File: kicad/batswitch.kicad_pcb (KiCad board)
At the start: 2 copper layers, 45.3 x 39.4 mm, 45 parts, among them J1 -VIN+, J2 -VOUT+, J3 DBG, J4 I2C_AUX, J5 I2C_DISP, Q1 SUD45P03-09, Q2 BSS84, Q3 SUD45P03-09, Q4 AO3401A, Q5 BSS138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

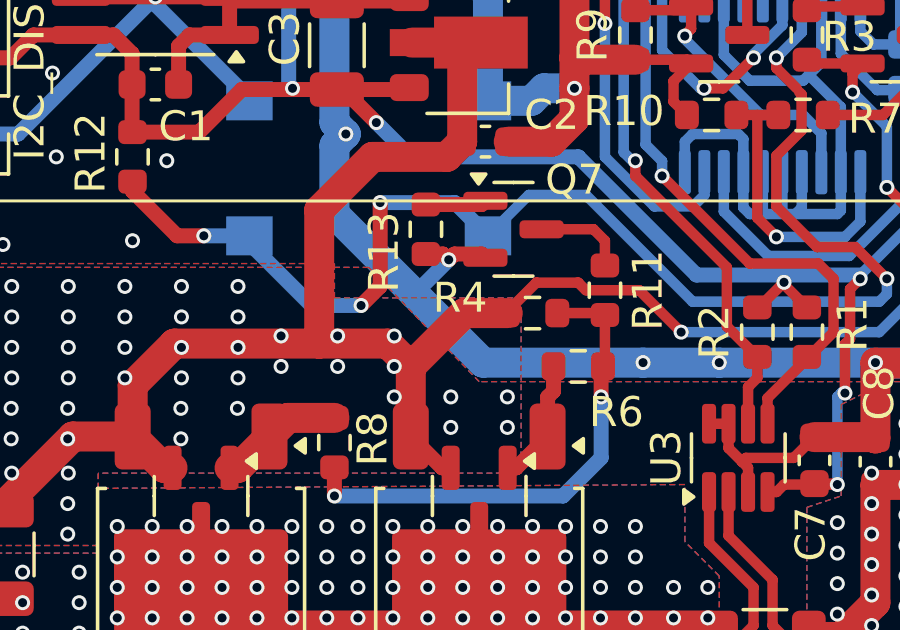
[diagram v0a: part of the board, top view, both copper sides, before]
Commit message: pcb: Fix ground plane
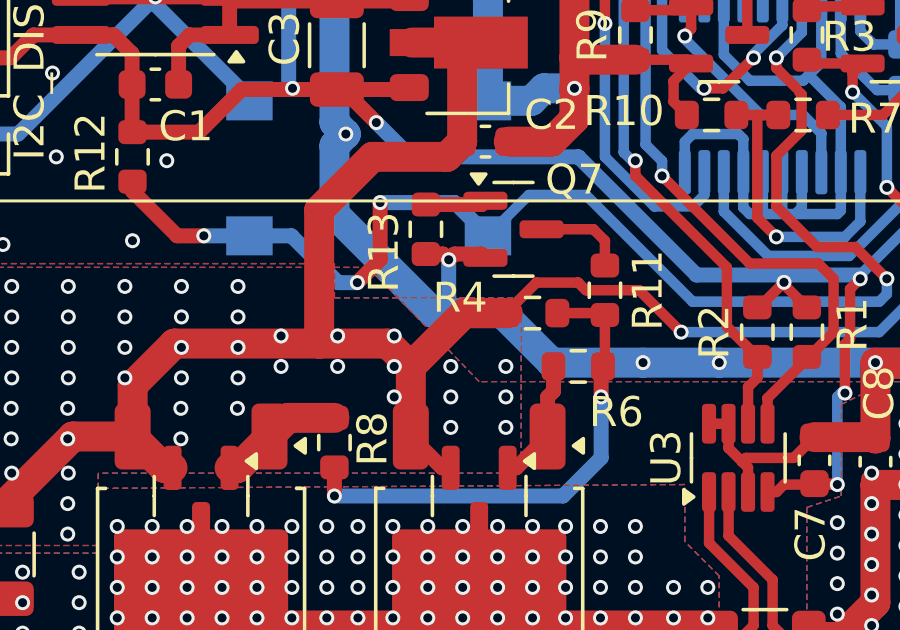
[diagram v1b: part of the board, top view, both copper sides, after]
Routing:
- net /BUTTON: track 45.8 -> 44.5 mm
- net /VIN: vias 57 -> 59
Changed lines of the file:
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@@
 		(tags "capacitor")
 		(property "Reference" "C2"
-			(at 2.205 -0.889 360)
+			(at 2.205 -0.889 0)
 			(layer "F.SilkS")
 			(effects
@@
 		)
 		(property "Value" "100nF"
-			(at 0 1.43 360)
+			(at 0 1.43 0)
 			(layer "F.Fab")
 			(effects
@@
 		)
 		(fp_text user "${REFERENCE}"
-			(at 0 0 360)
+			(at 0 0 0)
 			(layer "F.Fab")
 			(effects
@@
 	)
 	(gr_line
-		(start 70.612 81.026)
-		(end 73.914 80.518)
+		(start 68.072 82.169)
+		(end 70.612 81.026)
 		(stroke
 			(width 0.1)
@@
 	)
 	(gr_line
-		(start 68.072 82.169)
-		(end 70.612 81.026)
+		(start 70.612 81.026)
+		(end 73.914 80.518)
 		(stroke
 			(width 0.1)
@@
 	)
 	(via
+		(at 63.949791 98.171)
+		(size 0.5)
+		(drill 0.3)
+		(layers "F.Cu" "B.Cu")
+		(free yes)
+		(net 1)
+	)
+	(via
+		(at 65.786 98.171)
+		(size 0.5)
+		(drill 0.3)
+		(layers "F.Cu" "B.Cu")
+		(free yes)
+		(net 1)
+	)
+	(via
 		(at 62.064194 98.171)
 		(size 0.5)
@@
 	)
 	(via
-		(at 65.835388 100.203)
+		(at 65.786 100.203)
 		(size 0.5)
 		(drill 0.3)
@@
 	)
 	(via
-		(at 65.835388 99.187)
+		(at 65.786 99.187)
 		(size 0.5)
 		(drill 0.3)
@@
 	)
 	(segment
+		(start 60.071 93.091)
+		(end 60.071 90.805)
+		(width 1)
+		(layer "B.Cu")
+		(net 2)
+	)
+	(segment
 		(start 57.239 89.243)
 		(end 54.102 86.106)
@@
 	)
 	(segment
+		(start 67.31 98.044)
+		(end 70.358 98.044)
+		(width 1)
+		(layer "B.Cu")
+		(net 2)
+	)
+	(segment
 		(start 75.7525 83.1185)
 		(end 75.565 82.931)
@@
 	)
 	(segment
-		(start 60.071 93.091)
-		(end 60.071 90.805)
-		(width 1)
-		(layer "B.Cu")
-		(net 2)
-	)
-	(segment
 		(start 68.072 88.9)
 		(end 67.056 88.9)
@@
 	)
 	(segment
+		(start 63.373 96.393)
+		(end 63.881 95.885)
+		(width 0.5)
+		(layer "B.Cu")
+		(net 2)
+	)
+	(segment
 		(start 57.239 89.317)
 		(end 57.239 89.243)
@@
 	)
 	(segment
+		(start 63.373 96.393)
+		(end 60.071 93.091)
+		(width 1)
+		(layer "B.Cu")
+		(net 2)
+	)
+	(segment
 		(start 74.816 84.188)
 		(end 74.816 83.1185)
@@
 	)
 	(segment
+		(start 63.881 95.885)
+		(end 63.881 94.615)
+		(width 0.5)
+		(layer "B.Cu")
+		(net 2)
+	)
+	(segment
 		(start 54.102 85.852)
 		(end 49.53 90.424)
@@
 	)
 	(segment
-		(start 84.709 98.044)
-		(end 72.898 98.044)
+		(start 63.373 96.393)
+		(end 65.659 96.393)
 		(width 1)
 		(layer "B.Cu")
@@
 	)
 	(segment
-		(start 60.071 90.805)
-		(end 60.452 90.424)
+		(start 84.709 98.044)
+		(end 72.898 98.044)
 		(width 1)
 		(layer "B.Cu")
@@
 	)
 	(segment
-		(start 62.8015 95.8215)
-		(end 60.071 93.091)
-		(width 1)
-		(layer "B.Cu")
-		(net 2)
-	)
-	(segment
 		(start 85.868 99.203)
 		(end 84.709 98.044)
@@
 	)
 	(segment
-		(start 62.8015 95.6945)
-		(end 62.8015 95.8215)
-		(width 0.5)
-		(layer "B.Cu")
-		(net 2)
-	)
-	(segment
-		(start 70.358 98.044)
-		(end 65.024 98.044)
-		(width 1)
-		(layer "B.Cu")
-		(net 2)
-	)
-	(segment
 		(start 72.898 98.044)
 		(end 70.358 98.044)
@@
 	)
 	(segment
-		(start 65.024 98.044)
-		(end 62.8015 95.8215)
+		(start 65.659 96.393)
+		(end 67.31 98.044)
+		(width 1)
+		(layer "B.Cu")
+		(net 2)
+	)
+	(segment
+		(start 60.071 90.805)
+		(end 60.452 90.424)
 		(width 1)
 		(layer "B.Cu")
@@
 	)
 	(segment
-		(start 63.881 94.615)
-		(end 62.8015 95.6945)
-		(width 0.5)
-		(layer "B.Cu")
-		(net 2)
-	)
-	(segment
 		(start 44.069 87.884)
 		(end 47.879 87.884)
@@
 	)
 	(segment
+		(start 60.833 95.377)
+		(end 61.595 94.615)
+		(width 0.5)
+		(layer "F.Cu")
+		(net 13)
+	)
+	(segment
 		(start 78.486 95.25)
 		(end 77.428 94.192)
@@
 	)
 	(segment
-		(start 60.96 96.139)
-		(end 61.595 95.504)
-		(width 0.5)
-		(layer "F.Cu")
-		(net 13)
-	)
-	(segment
 		(start 53.34 92.011)
 		(end 53.34 92.329)
@@
 	)
 	(segment
-		(start 61.595 95.504)
+		(start 61.595 94.615)
 		(end 61.595 92.71)
 		(width 0.5)
@@
 	)
 	(via
-		(at 60.96 96.139)
+		(at 60.833 95.377)
 		(size 0.5)
 		(drill 0.3)
@@
 	)
 	(segment
-		(start 57.239 93.817)
-		(end 57.239 94.069)
-		(width 0.5)
-		(layer "B.Cu")
-		(net 13)
-	)
-	(segment
 		(start 66.55 92.456)
 		(end 65.189 93.817)
@@
 	)
 	(segment
-		(start 59.309 96.139)
-		(end 60.96 96.139)
-		(width 0.5)
-		(layer "B.Cu")
-		(net 13)
-	)
-	(segment
 		(start 78.486 95.758)
 		(end 78.232 96.012)
@@
 	)
 	(segment
-		(start 75.651 87.036)
-		(end 74.803 87.884)
-		(width 0.35)
+		(start 60.198 95.377)
+		(end 58.638 93.817)
+		(width 0.5)
 		(layer "B.Cu")
 		(net 13)
 	)
 	(segment
-		(start 57.239 94.069)
-		(end 59.309 96.139)
-		(width 0.5)
+		(start 75.651 87.036)
+		(end 74.803 87.884)
+		(width 0.35)
 		(layer "B.Cu")
 		(net 13)
@@
 	)
 	(segment
+		(start 60.833 95.377)
+		(end 60.198 95.377)
+		(width 0.5)
+		(layer "B.Cu")
+		(net 13)
+	)
+	(segment
 		(start 75.651 85.971)
 		(end 75.651 87.036)
@@
 		(layer "B.Cu")
 		(net 13)
+	)
+	(segment
+		(start 58.638 93.817)
+		(end 57.239 93.817)
+		(width 0.5)
+		(layer "B.Cu")
+		(net 13)
